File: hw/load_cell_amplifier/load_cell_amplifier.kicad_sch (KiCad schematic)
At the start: 8 parts, among them U1 INA129, U2 TL072

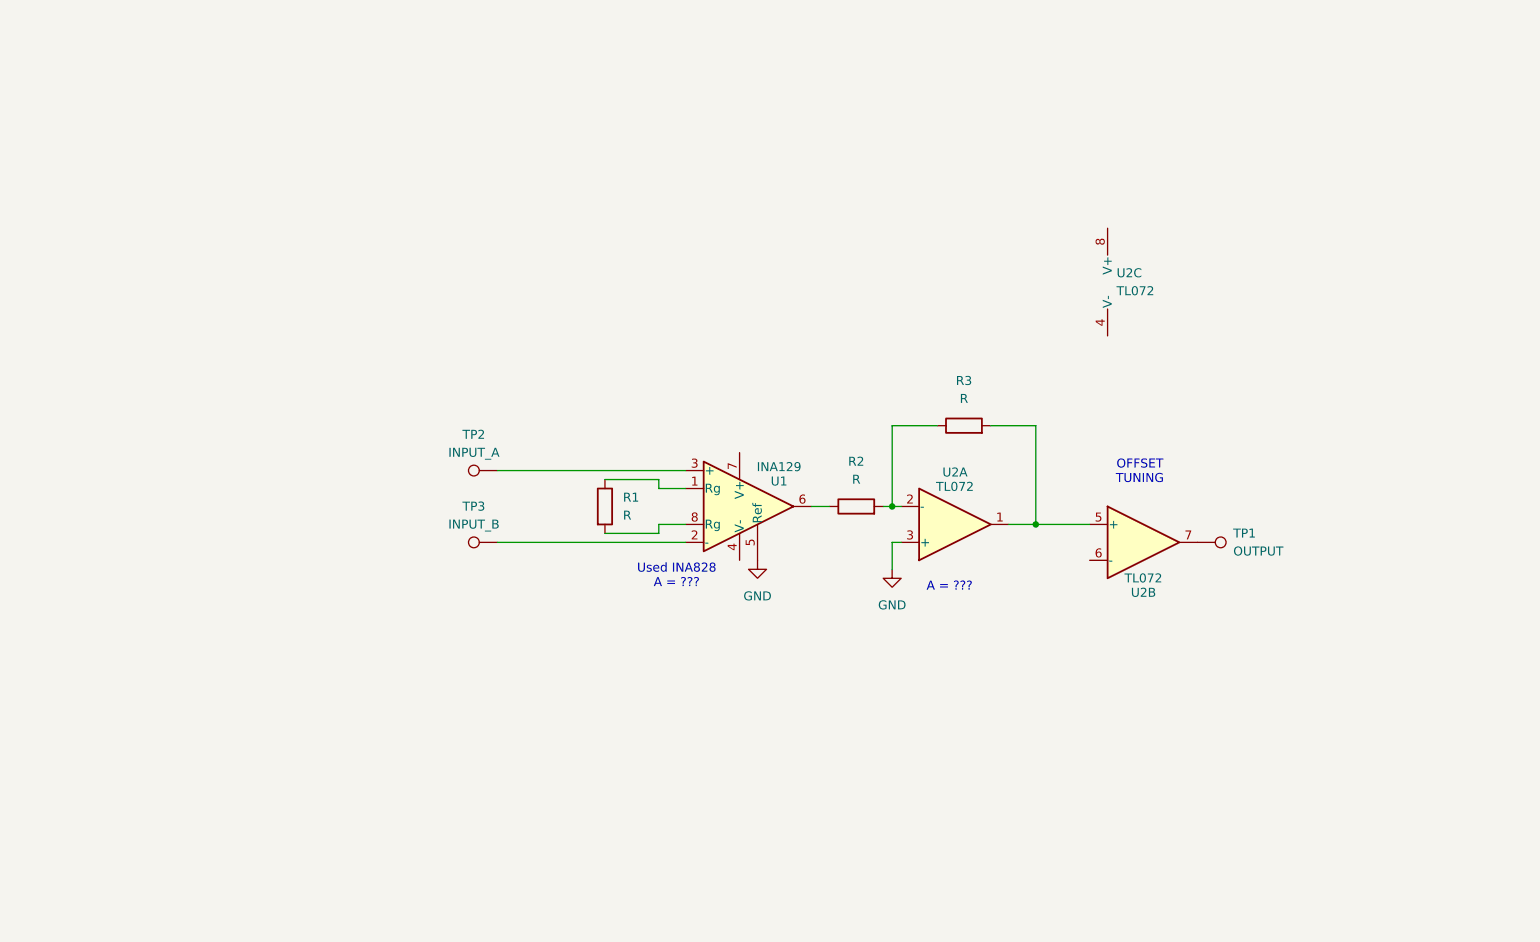
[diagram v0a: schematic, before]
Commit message: updated contact array circuit
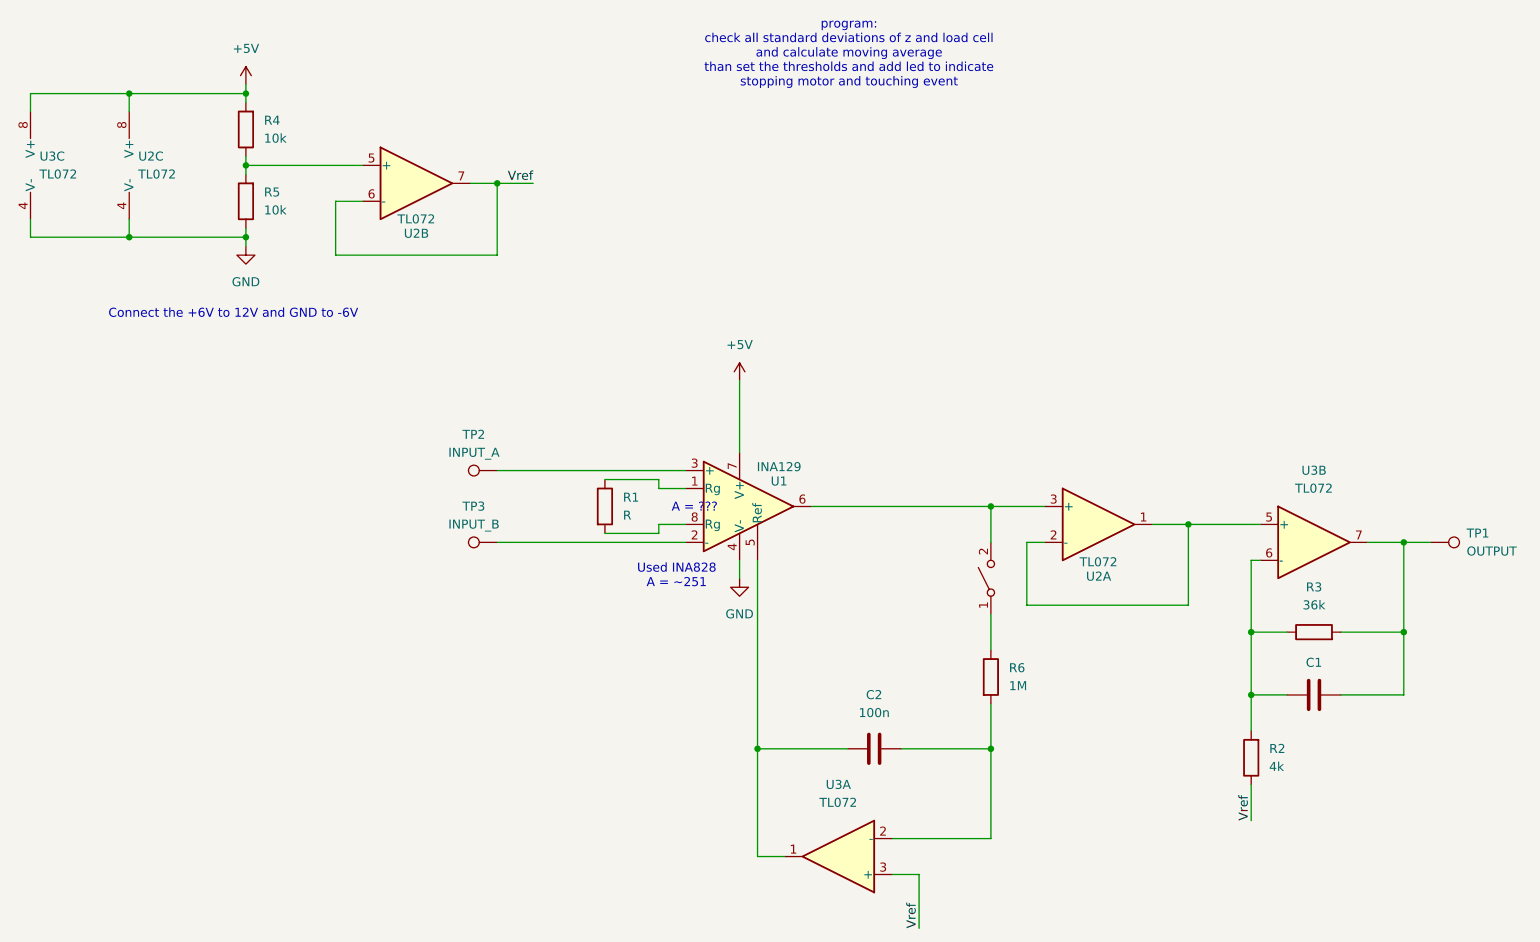
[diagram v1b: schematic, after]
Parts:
- added C1: 200n, symbol Device:C
- added C2: 100n, symbol Device:C
- added R4, R5: 10k, symbol Device:R
- added R6: 1M, symbol Device:R
- added SW1: SW_DPST_x2, symbol Switch:SW_DPST_x2
- added U3: TL072, symbol Amplifier_Operational:TL072
- R2: value R -> 4k
- R3: value R -> 36k
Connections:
- net GND: now also U1.4 (V-), U2.4 (V-), R5.1, U3.4 (V-); no longer U1.5 (Ref), U2.3 (+)
- net at R2.2, R3.1: now also C1.1, U3.6 (-); no longer U2.2 (-)
- net at U1.6: now also U2.3 (+), SW1.2 (B); no longer R2.1
- net +5V: now reaches U1.7 (V+)
- net +5V: now also U2.8 (V+), R4.2, U3.8 (V+)
- net at TP1.1: now also R3.2, C1.2, U3.7; no longer U2.7
- net Vref: now reaches U2.6 (-)
- net Vref: now also R2.1, U2.7, U3.3 (+)
- new net: C2.1, U1.5 (Ref), U3.1
- new net: U2.1, U2.2 (-), U3.5 (+)
- new net: C2.2, R6.2, U3.2 (-)
- new net: R6.1, SW1.1 (A)
- new net: R4.1, R5.2, U2.5 (+)
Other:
- note added: "Connect the +6V to 12V and GND to -6V"
- note added: "Used INA828 A = ~251"
- note added: "program: check all standard deviations of z and load cell and calculate moving average than set the thresholds and add led to indicate stopping motor and touching event"
- note removed: "OFFSET TUNING"
- note removed: "Used INA828 A = ???"
- moved on the sheet: R2, R3, TP1, U2A, U2B, U2C
